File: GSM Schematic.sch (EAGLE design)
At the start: 19 parts, among them IC1 7805T, J1 5.5x2.1mm Barrel, J2 AVR_SPI_PRG_62X3_LOCK, Q2 16M, U1 ATMEGA328P-PU

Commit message: updated the Schematic and changed PCB layout
Updated the Schematic and included a surface mount for the Voltage regulator and changed the layout of the PCB and added a logo to it
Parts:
- removed IC1: 7805T, linear:7805T
- added U2: LM317MDT-TR, MF_IC_Power:LM317MDT-TR
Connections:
- net 12V: now also U2.VIN; no longer IC1.VI
- net 5V: now also U2.VOUT; no longer IC1.VO
- net GND: now also U2.GND/ADJ; no longer IC1.GND
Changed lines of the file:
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@@
 <setting verticaltext="up"/>
 </settings>
-<grid distance="0.05" unitdist="inch" unit="inch" style="lines" multiple="2" display="yes" altdistance="0.01" altunitdist="inch" altunit="inch"/>
+<grid distance="0.1" unitdist="inch" unit="inch" style="lines" multiple="1" display="no" altdistance="0.01" altunitdist="inch" altunit="inch"/>
 <layers>
 <layer number="1" name="Top" color="4" fill="1" visible="no" active="no"/>
@@
 <parts>
 <part name="U1" library="Atmel_By_element14_Batch_1-00" deviceset="ATMEGA328P-PU" device=""/>
-<part name="IC1" library="linear" deviceset="78*" device="T" technology="05"/>
 <part name="GND1" library="supply1" deviceset="GND" device=""/>
 <part name="GND2" library="supply1" deviceset="GND" device=""/>
@@
 <part name="C5" library="rcl" deviceset="CPOL-EU" device="E5-10.5" value="10u"/>
 <part name="LED3" library="led" deviceset="LED" device="5MM"/>
+<part name="U2" library="MF_IC_Power" deviceset="LM317" device="MDT-TR" value="LM317MDT-TR"/>
 </parts>
 <sheets>
@@
 <attribute name="VALUE" x="224.8916" y="126.4412" size="2.0828" layer="96" ratio="10" rot="SR0"/>
 </instance>
-<instance part="IC1" gate="A1" x="175.26" y="205.74"/>
 <instance part="GND1" gate="1" x="175.26" y="193.04"/>
 <instance part="GND2" gate="1" x="185.42" y="161.29" smashed="yes">
@@
 <instance part="C5" gate="G$1" x="187.96" y="203.2"/>
 <instance part="LED3" gate="G$1" x="295.91" y="149.86" rot="R90"/>
+<instance part="U2" gate="G$1" x="170.18" y="205.74"/>
 </instances>
 <busses>
@@
 </segment>
 <segment>
-<pinref part="IC1" gate="A1" pin="GND"/>
 <pinref part="GND1" gate="1" pin="GND"/>
 <wire x1="175.26" y1="198.12" x2="175.26" y2="195.58" width="0.1524" layer="91"/>
@@
 <junction x="175.26" y="195.58"/>
 <pinref part="C3" gate="G$1" pin="-"/>
+<pinref part="U2" gate="G$1" pin="GND/ADJ"/>
 </segment>
 <segment>
@@
 <net name="5V" class="0">
 <segment>
-<pinref part="IC1" gate="A1" pin="VO"/>
-<wire x1="185.42" y1="205.74" x2="187.96" y2="205.74" width="0.1524" layer="91"/>
 <wire x1="187.96" y1="205.74" x2="195.58" y2="205.74" width="0.1524" layer="91"/>
 <wire x1="195.58" y1="205.74" x2="195.58" y2="185.42" width="0.1524" layer="91"/>
@@
 <wire x1="218.44" y1="172.72" x2="195.58" y2="172.72" width="0.1524" layer="91"/>
 <junction x="195.58" y="172.72"/>
+<pinref part="U2" gate="G$1" pin="VOUT"/>
+<wire x1="182.88" y1="205.74" x2="187.96" y2="205.74" width="0.1524" layer="91"/>
 </segment>
 </net>
@@
 <net name="12V" class="0">
 <segment>
-<pinref part="IC1" gate="A1" pin="VI"/>
-<wire x1="160.02" y1="205.74" x2="165.1" y2="205.74" width="0.1524" layer="91"/>
+<wire x1="160.02" y1="205.74" x2="167.64" y2="205.74" width="0.1524" layer="91"/>
 <junction x="160.02" y="205.74"/>
 <pinref part="J1" gate="G$1" pin="PWR"/>
@@
 <junction x="276.86" y="142.24"/>
 <pinref part="C3" gate="G$1" pin="+"/>
-</segment>
-</net>
+<pinref part="U2" gate="G$1" pin="VIN"/>
+</segment>
+</net>

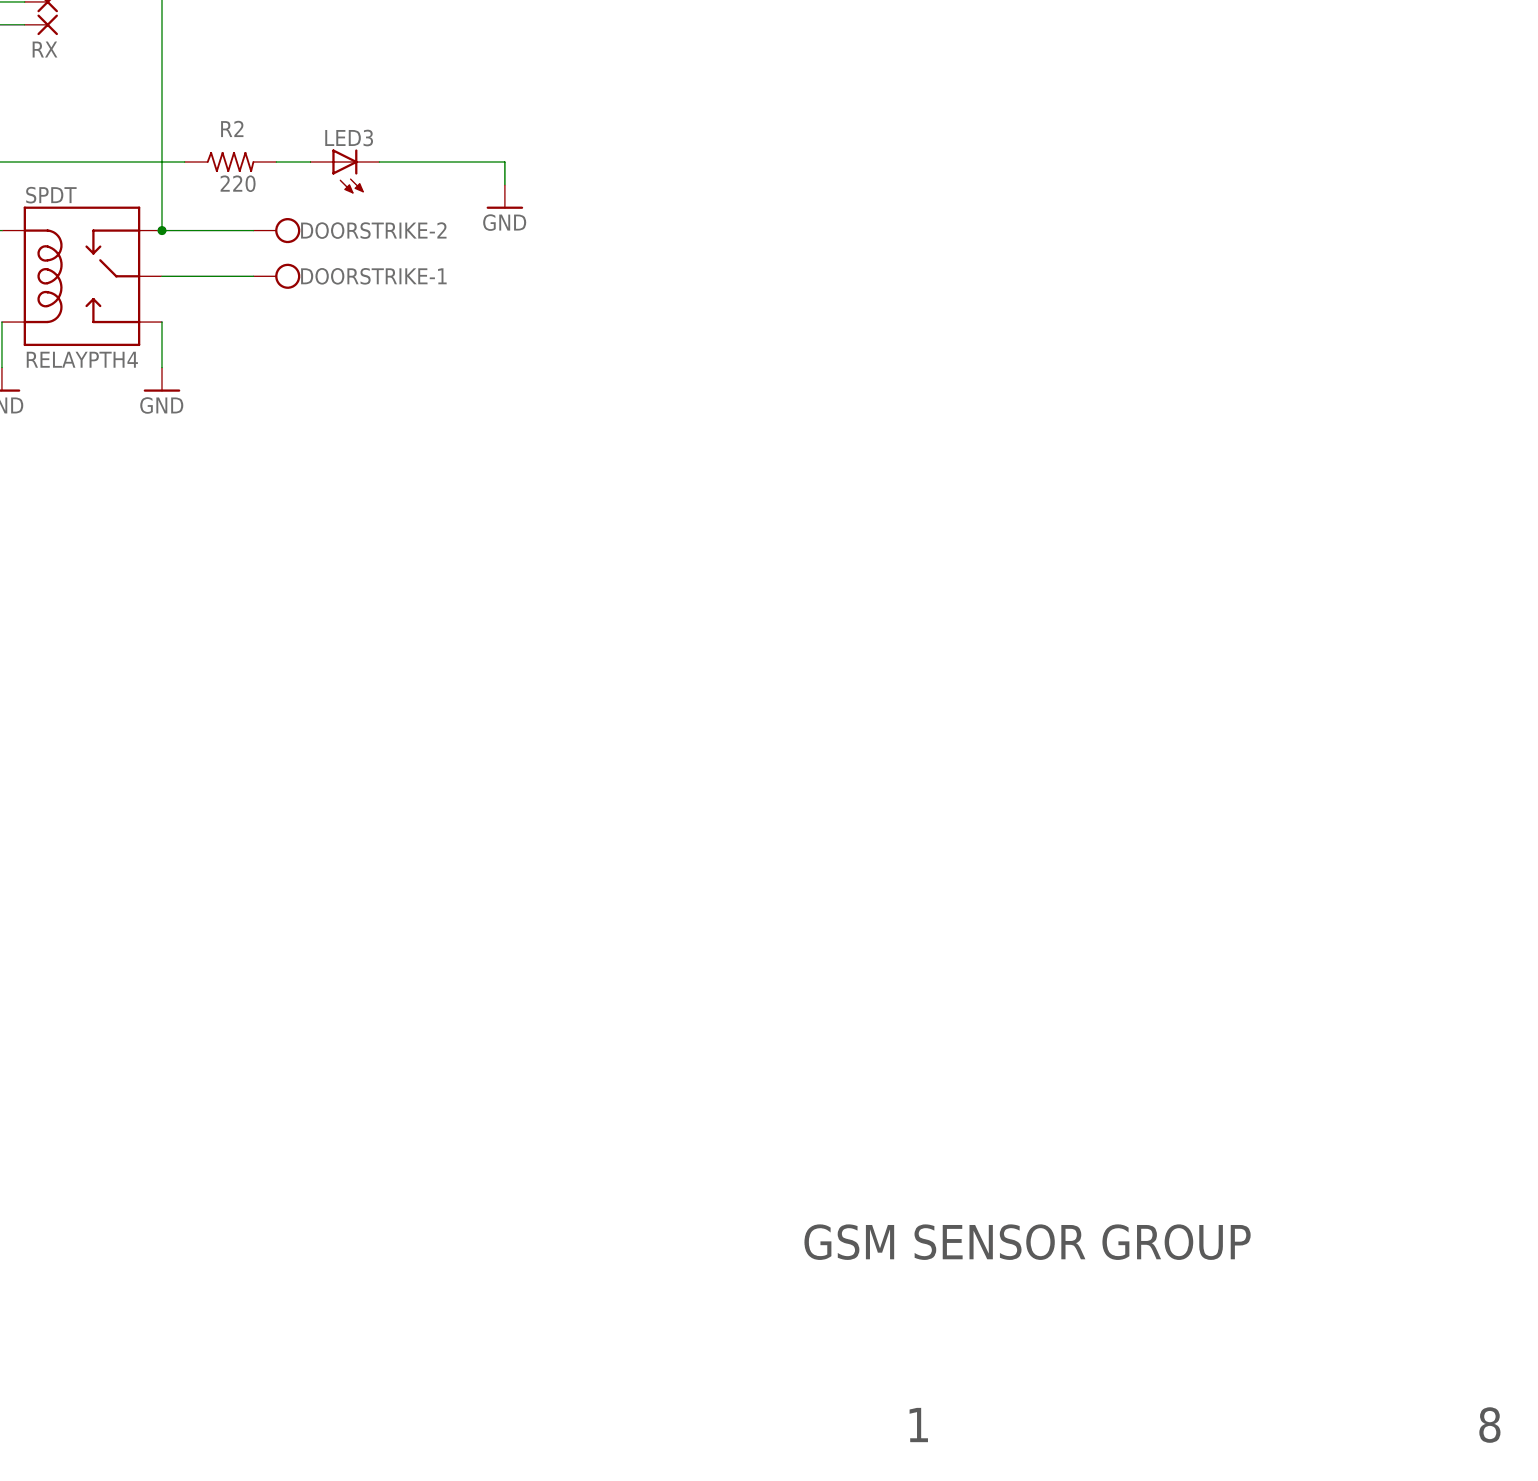
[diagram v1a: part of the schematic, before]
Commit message: Add files via upload
Added diode to door strike output and cleaned up breadboard lines.
Also solved consistency errors
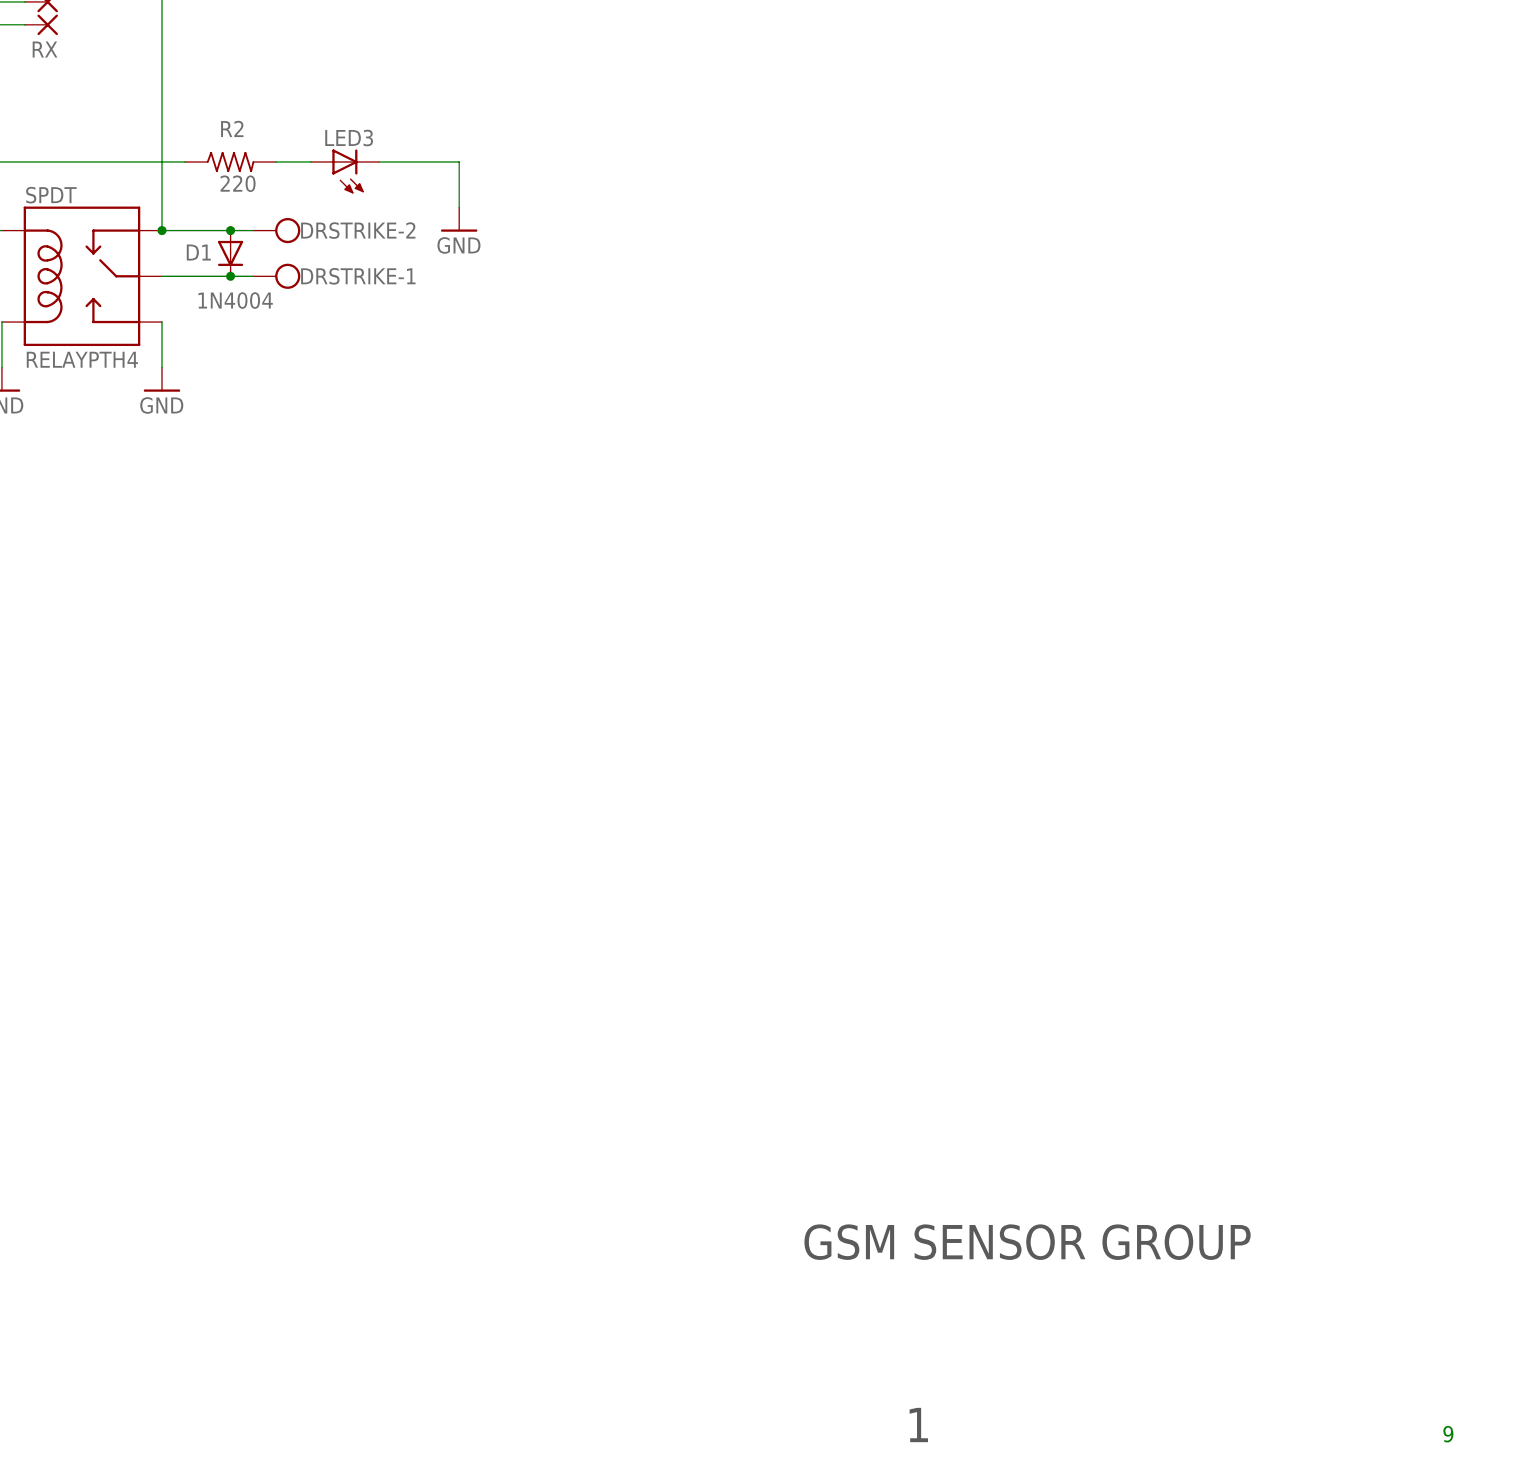
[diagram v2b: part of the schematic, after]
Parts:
- added D1: 1N4004, diode:1N4004
- renumbered DOORSTRIKE to DRSTRIKE
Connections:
- net 12V: now also D1.A
- net N$4: now also D1.C
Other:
- note added: "9"
- note removed: "8"
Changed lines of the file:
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@@
 <?xml version="1.0" encoding="utf-8"?>
 <!DOCTYPE eagle SYSTEM "eagle.dtd">
-<eagle version="7.7.0">
+<eagle version="7.6.0">
 <drawing>
 <settings>
@@
 <setting verticaltext="up"/>
 </settings>
-<grid distance="0.1" unitdist="inch" unit="inch" style="lines" multiple="1" display="no" altdistance="0.01" altunitdist="inch" altunit="inch"/>
+<grid distance="0.05" unitdist="inch" unit="inch" style="lines" multiple="2" display="yes" altdistance="0.01" altunitdist="inch" altunit="inch"/>
 <layers>
 <layer number="1" name="Top" color="4" fill="1" visible="no" active="no"/>
@@
 <part name="GND10" library="supply1" deviceset="GND" device=""/>
 <part name="GND11" library="supply1" deviceset="GND" device=""/>
-<part name="DOORSTRIKE" library="con-wago-500" deviceset="W237-102" device=""/>
+<part name="DRSTRIKE" library="con-wago-500" deviceset="W237-102" device=""/>
 <part name="R2" library="rcl" deviceset="R-US_" device="R0603" value="220"/>
 <part name="GND5" library="supply1" deviceset="GND" device=""/>
@@
 <part name="LED3" library="led" deviceset="LED" device="5MM"/>
 <part name="U2" library="MF_IC_Power" deviceset="LM317" device="MDT-TR" value="LM317MDT-TR"/>
+<part name="D1" library="diode" deviceset="1N4004" device=""/>
 </parts>
 <sheets>
@@
 <plain>
 <text x="359.41" y="7.62" size="3.81" layer="97" font="vector">1</text>
-<text x="422.91" y="7.62" size="3.81" layer="97" font="vector">8</text>
 <text x="347.98" y="27.94" size="3.81" layer="97" font="vector">GSM SENSOR GROUP</text>
+<text x="419.1" y="7.62" size="1.778" layer="91">9</text>
 </plain>
 <instances>
@@
 <instance part="GND10" gate="1" x="203.2" y="101.6"/>
 <instance part="GND11" gate="1" x="213.36" y="101.6"/>
-<instance part="DOORSTRIKE" gate="-1" x="292.1" y="137.16" rot="R180"/>
-<instance part="DOORSTRIKE" gate="-2" x="292.1" y="142.24" rot="R180"/>
+<instance part="DRSTRIKE" gate="-1" x="292.1" y="137.16" rot="R180"/>
+<instance part="DRSTRIKE" gate="-2" x="292.1" y="142.24" rot="R180"/>
 <instance part="R2" gate="G$1" x="284.48" y="149.86" smashed="yes">
 <attribute name="NAME" x="283.21" y="152.6286" size="1.778" layer="95"/>
 <attribute name="VALUE" x="283.21" y="146.558" size="1.778" layer="96"/>
 </instance>
-<instance part="GND5" gate="1" x="314.96" y="144.78" smashed="yes">
-<attribute name="VALUE" x="312.42" y="142.24" size="1.778" layer="96"/>
+<instance part="GND5" gate="1" x="309.88" y="142.24" smashed="yes">
+<attribute name="VALUE" x="307.34" y="139.7" size="1.778" layer="96"/>
 </instance>
 <instance part="C3" gate="G$1" x="160.02" y="203.2"/>
@@
 <instance part="LED3" gate="G$1" x="295.91" y="149.86" rot="R90"/>
 <instance part="U2" gate="G$1" x="170.18" y="205.74"/>
+<instance part="D1" gate="1" x="284.48" y="139.7" smashed="yes" rot="R270">
+<attribute name="NAME" x="279.4" y="138.9126" size="1.778" layer="95"/>
+<attribute name="VALUE" x="280.67" y="133.5786" size="1.778" layer="96"/>
+</instance>
 </instances>
 <busses>
@@
 </segment>
 <segment>
-<wire x1="300.99" y1="149.86" x2="314.96" y2="149.86" width="0.1524" layer="91"/>
-<wire x1="314.96" y1="149.86" x2="314.96" y2="147.32" width="0.1524" layer="91"/>
+<wire x1="300.99" y1="149.86" x2="309.88" y2="149.86" width="0.1524" layer="91"/>
+<wire x1="309.88" y1="149.86" x2="309.88" y2="144.78" width="0.1524" layer="91"/>
 <pinref part="GND5" gate="1" pin="GND"/>
 <pinref part="LED3" gate="G$1" pin="C"/>
@@
 <wire x1="160.02" y1="215.9" x2="276.86" y2="215.9" width="0.1524" layer="91"/>
 <wire x1="276.86" y1="215.9" x2="276.86" y2="142.24" width="0.1524" layer="91"/>
-<pinref part="DOORSTRIKE" gate="-2" pin="KL"/>
-<wire x1="287.02" y1="142.24" x2="276.86" y2="142.24" width="0.1524" layer="91"/>
+<pinref part="DRSTRIKE" gate="-2" pin="KL"/>
+<wire x1="287.02" y1="142.24" x2="284.48" y2="142.24" width="0.1524" layer="91"/>
 <junction x="276.86" y="142.24"/>
 <pinref part="C3" gate="G$1" pin="+"/>
 <pinref part="U2" gate="G$1" pin="VIN"/>
+<pinref part="D1" gate="1" pin="A"/>
+<wire x1="284.48" y1="142.24" x2="276.86" y2="142.24" width="0.1524" layer="91"/>
+<junction x="284.48" y="142.24"/>
 </segment>
 </net>
@@
 <segment>
 <pinref part="SPDT" gate="K$1" pin="MAIN"/>
-<pinref part="DOORSTRIKE" gate="-1" pin="KL"/>
-<wire x1="287.02" y1="137.16" x2="276.86" y2="137.16" width="0.1524" layer="91"/>
-</segment>
-</net>
+<pinref part="DRSTRIKE" gate="-1" pin="KL"/>
+<wire x1="287.02" y1="137.16" x2="284.48" y2="137.16" width="0.1524" layer="91"/>
+<pinref part="D1" gate="1" pin="C"/>
+<wire x1="284.48" y1="137.16" x2="276.86" y2="137.16" width="0.1524" layer="91"/>
+<junction x="284.48" y="137.16"/>
+</segment>
+</net>
